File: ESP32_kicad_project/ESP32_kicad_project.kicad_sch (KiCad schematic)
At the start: 0 parts

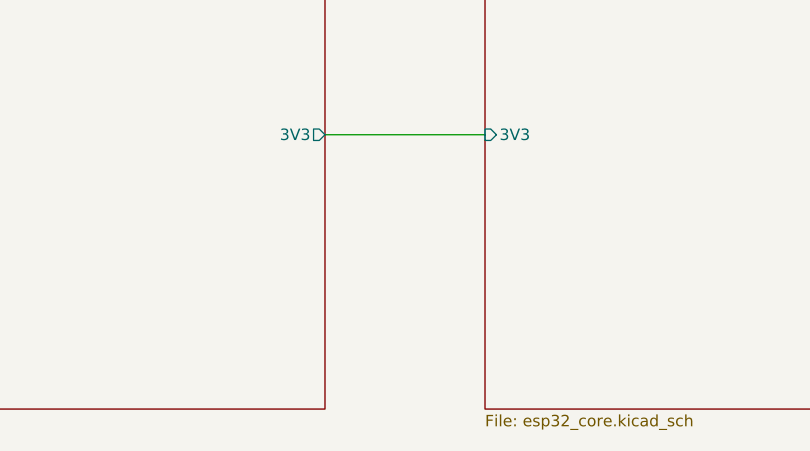
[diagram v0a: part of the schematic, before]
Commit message: added extra decoupling caps on the esp32 core 3V3 input
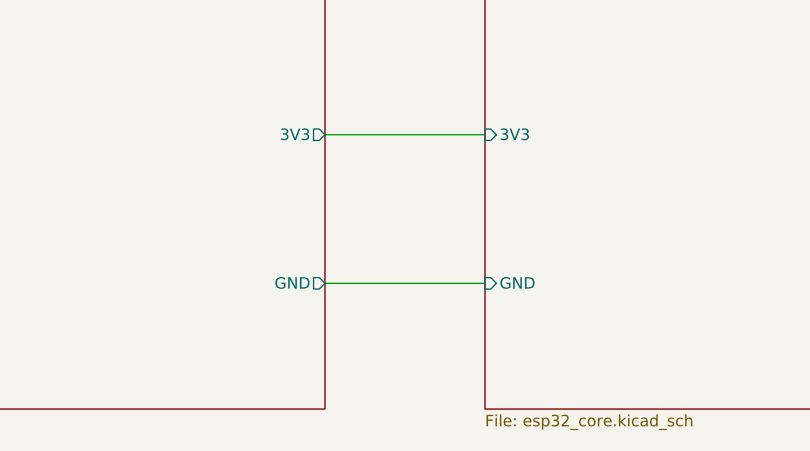
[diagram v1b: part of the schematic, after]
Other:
- sheet ESP32 Core ports: added GND; removed none
- sheet Power ports: added GND; removed none
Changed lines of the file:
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@@
+	(wire
+		(pts
+			(xy 93.98 62.23) (xy 111.76 62.23)
+		)
+		(stroke
+			(width 0)
+			(type default)
+		)
+	)
 	(wire
 		(pts
@@
 		(pin "3V3" input
 			(at 111.76 45.72 180)
+			(effects
+				(font
+					(size 1.27 1.27)
+				)
+				(justify left)
+			)
+		)
+		(pin "GND" input
+			(at 111.76 62.23 180)
 			(effects
 				(font
@@
 			(effects
 				(font
+					(size 1.27 1.27)
+				)
+				(justify right)
+			)
+		)
+		(pin "GND" output
+			(at 93.98 62.23 0)
+			(effects
+				(font

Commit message: completed core, moving on to the usb-uart core
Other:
- added sheet USB-UART (usb_uart.kicad_sch)
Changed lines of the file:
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@@
+		)
+	)
+	(sheet
+		(at 22.86 92.71)
+		(size 67.31 43.18)
+		(exclude_from_sim no)
+		(in_bom yes)
+		(on_board yes)
+		(dnp no)
+		(fields_autoplaced yes)
+		(stroke
+			(width 0.1524)
+			(type solid)
+		)
+		(fill
+			(color 0 0 0 0.0000)
+		)
+		(property "Sheetname" "USB-UART"
+			(at 22.86 91.9984 0)
+			(effects
+				(font
+					(size 1.27 1.27)
+				)
+				(justify left bottom)
+			)
+		)
+		(property "Sheetfile" "usb_uart.kicad_sch"
+			(at 22.86 136.4746 0)
+			(effects
+				(font
+					(size 1.27 1.27)
+				)
+				(justify left top)
+			)
+		)
+		(instances
+			(project "ESP32_kicad_project"
+				(path "/8f7d6ecf-e535-4443-9266-fe4b2e9314d5"
+					(page "4")
+				)
+			)
 		)
 	)

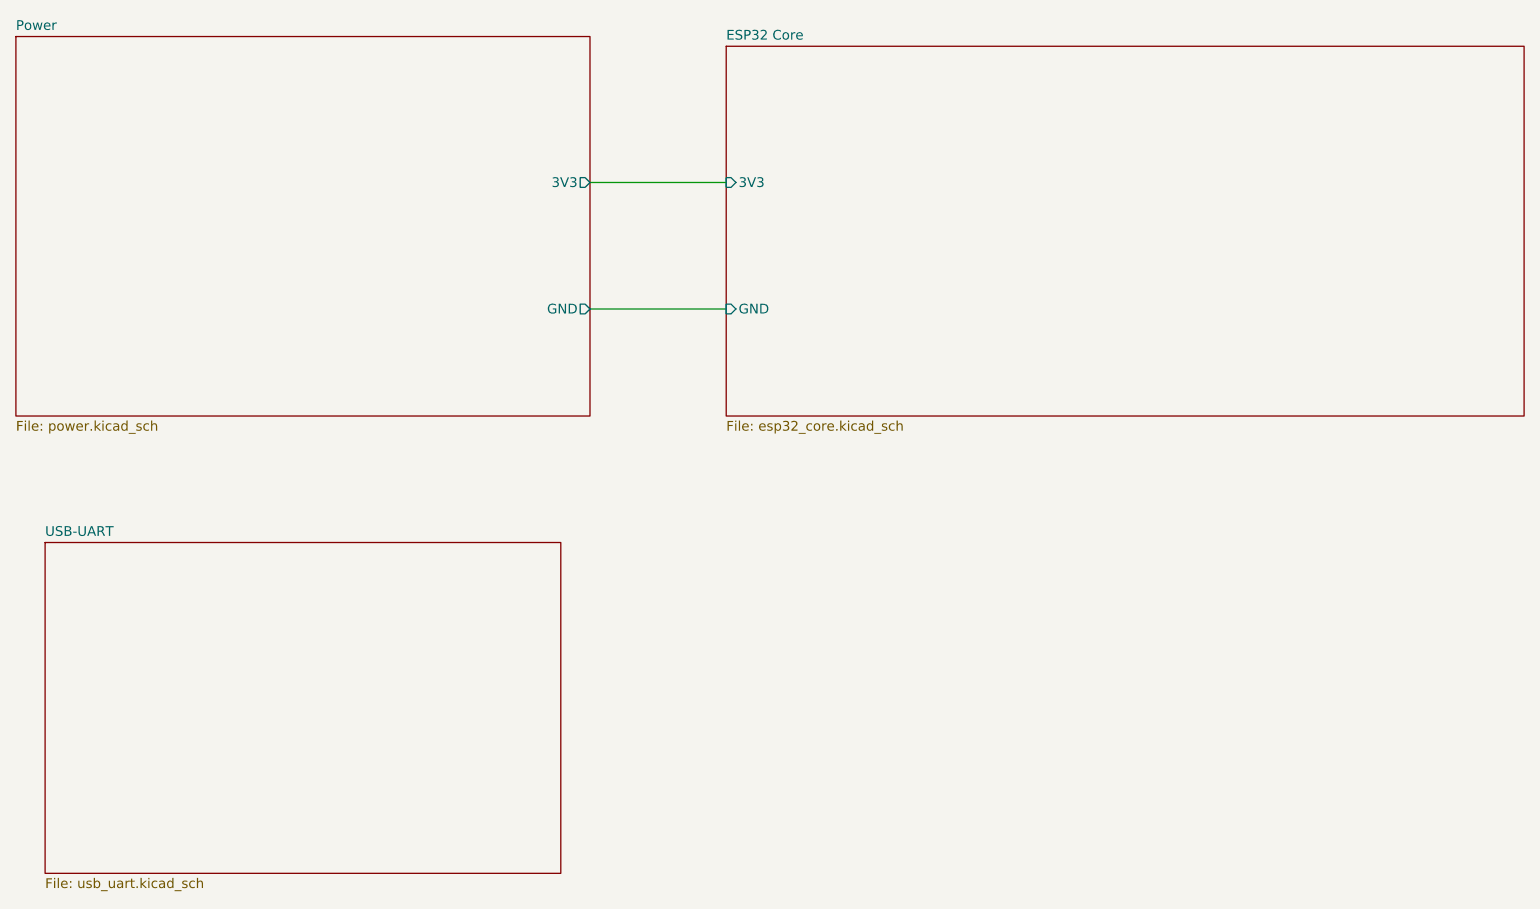
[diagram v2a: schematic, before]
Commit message: added USB chip, implemented ESP32 auto reset DTR RTS circuit
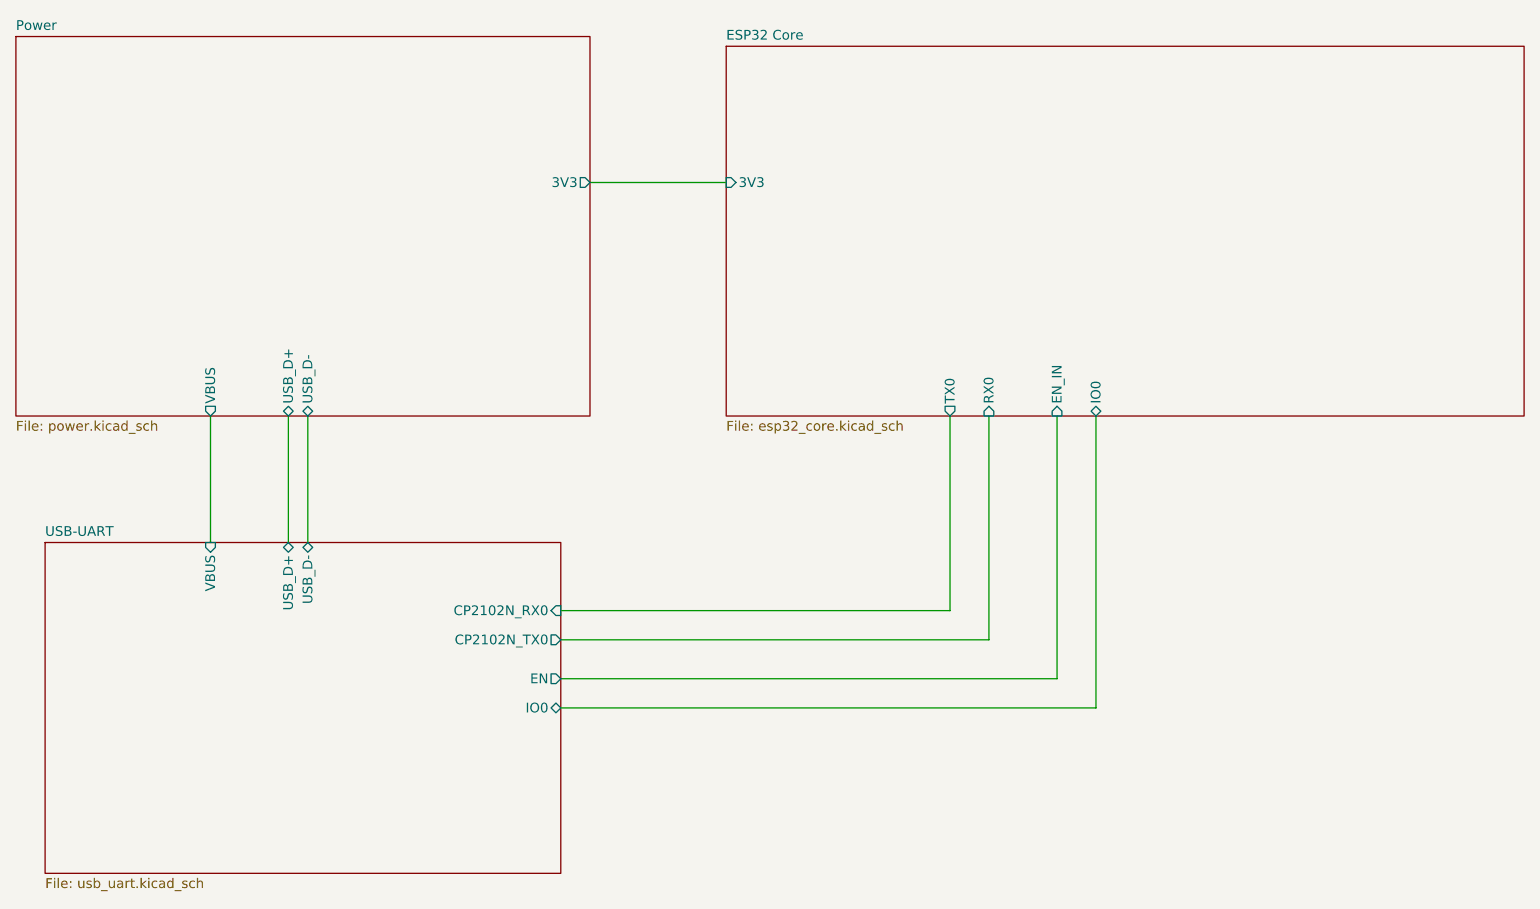
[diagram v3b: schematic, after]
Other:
- sheet ESP32 Core ports: added EN_IN, IO0, RX0, TX0; removed GND
- sheet Power ports: added USB_D+, USB_D-, VBUS; removed GND
- sheet USB-UART ports: added CP2102N_RX0, CP2102N_TX0, EN, IO0, USB_D+, USB_D-, VBUS; removed none
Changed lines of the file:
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@@
 	(wire
 		(pts
-			(xy 93.98 62.23) (xy 111.76 62.23)
+			(xy 160.02 76.2) (xy 160.02 114.3)
+		)
+		(stroke
+			(width 0)
+			(type default)
+		)
+	)
+	(wire
+		(pts
+			(xy 44.45 76.2) (xy 44.45 92.71)
+		)
+		(stroke
+			(width 0)
+			(type default)
+		)
+	)
+	(wire
+		(pts
+			(xy 154.94 76.2) (xy 154.94 110.49)
+		)
+		(stroke
+			(width 0)
+			(type default)
+		)
+	)
+	(wire
+		(pts
+			(xy 140.97 101.6) (xy 90.17 101.6)
+		)
+		(stroke
+			(width 0)
+			(type default)
+		)
+	)
+	(wire
+		(pts
+			(xy 146.05 105.41) (xy 90.17 105.41)
+		)
+		(stroke
+			(width 0)
+			(type default)
+		)
+	)
+	(wire
+		(pts
+			(xy 154.94 110.49) (xy 90.17 110.49)
+		)
+		(stroke
+			(width 0)
+			(type default)
+		)
+	)
+	(wire
+		(pts
+			(xy 160.02 114.3) (xy 90.17 114.3)
+		)
+		(stroke
+			(width 0)
+			(type default)
+		)
+	)
+	(wire
+		(pts
+			(xy 140.97 76.2) (xy 140.97 101.6)
+		)
+		(stroke
+			(width 0)
+			(type default)
+		)
+	)
+	(wire
+		(pts
+			(xy 57.15 76.2) (xy 57.15 92.71)
+		)
+		(stroke
+			(width 0)
+			(type default)
+		)
+	)
+	(wire
+		(pts
+			(xy 146.05 76.2) (xy 146.05 105.41)
 		)
 		(stroke
@@
 		(pts
 			(xy 93.98 45.72) (xy 111.76 45.72)
+		)
+		(stroke
+			(width 0)
+			(type default)
+		)
+	)
+	(wire
+		(pts
+			(xy 54.61 76.2) (xy 54.61 92.71)
 		)
 		(stroke
@@
 			)
 		)
-		(pin "GND" input
-			(at 111.76 62.23 180)
+		(pin "TX0" output
+			(at 140.97 76.2 270)
+			(effects
+				(font
+					(size 1.27 1.27)
+				)
+				(justify left)
+			)
+		)
+		(pin "RX0" input
+			(at 146.05 76.2 270)
+			(effects
+				(font
+					(size 1.27 1.27)
+				)
+				(justify left)
+			)
+		)
+		(pin "IO0" bidirectional
+			(at 160.02 76.2 270)
+			(effects
+				(font
+					(size 1.27 1.27)
+				)
+				(justify left)
+			)
+		)
+		(pin "EN_IN" input
+			(at 154.94 76.2 270)
 			(effects
 				(font
@@
 			)
 		)
-		(pin "GND" output
-			(at 93.98 62.23 0)
-			(effects
-				(font
-					(size 1.27 1.27)
-				)
-				(justify right)
+		(pin "VBUS" output
+			(at 44.45 76.2 270)
+			(effects
+				(font
+					(size 1.27 1.27)
+				)
+				(justify left)
+			)
+		)
+		(pin "USB_D+" bidirectional
+			(at 54.61 76.2 270)
+			(effects
+				(font
+					(size 1.27 1.27)
+				)
+				(justify left)
+			)
+		)
+		(pin "USB_D-" bidirectional
+			(at 57.15 76.2 270)
+			(effects
+				(font
+					(size 1.27 1.27)
+				)
+				(justify left)
 			)
 		)
@@
 			)
 		)
+		(pin "VBUS" input
+			(at 44.45 92.71 90)
+			(effects
+				(font
+					(size 1.27 1.27)
+				)
+				(justify right)
+			)
+		)
+		(pin "USB_D-" bidirectional
+			(at 57.15 92.71 90)
+			(effects
+				(font
+					(size 1.27 1.27)
+				)
+				(justify right)
+			)
+		)
+		(pin "USB_D+" bidirectional
+			(at 54.61 92.71 90)
+			(effects
+				(font
+					(size 1.27 1.27)
+				)
+				(justify right)
+			)
+		)
+		(pin "CP2102N_RX0" input
+			(at 90.17 101.6 0)
+			(effects
+				(font
+					(size 1.27 1.27)
+				)
+				(justify right)
+			)
+		)
+		(pin "CP2102N_TX0" output
+			(at 90.17 105.41 0)
+			(effects
+				(font
+					(size 1.27 1.27)
+				)
+				(justify right)
+			)
+		)
+		(pin "EN" output
+			(at 90.17 110.49 0)
+			(effects
+				(font
+					(size 1.27 1.27)
+				)
+				(justify right)
+			)
+		)
+		(pin "IO0" bidirectional
+			(at 90.17 114.3 0)
+			(effects
+				(font
+					(size 1.27 1.27)
+				)
+				(justify right)
+			)
+		)

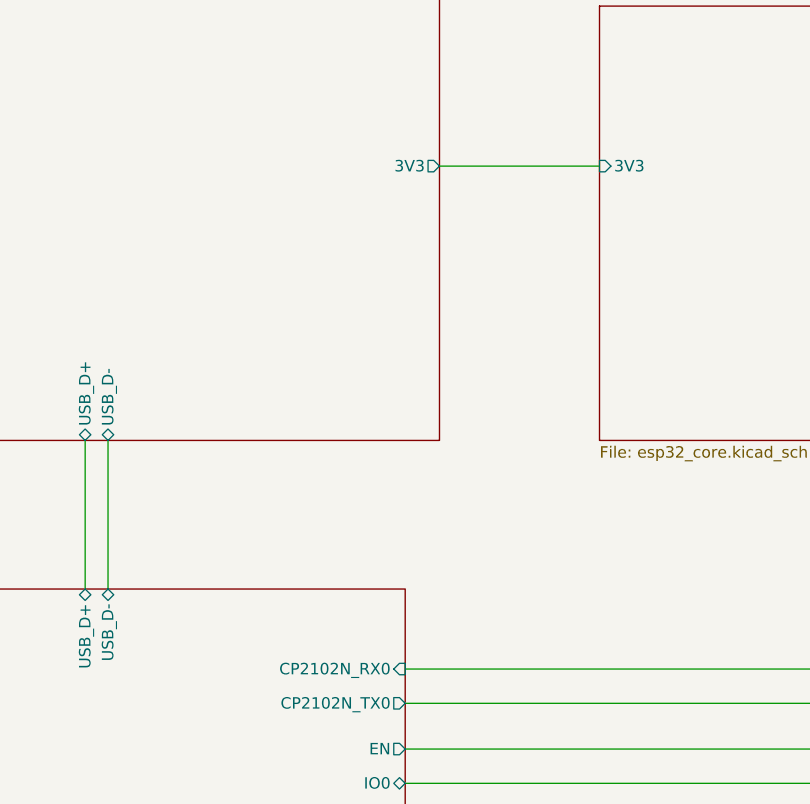
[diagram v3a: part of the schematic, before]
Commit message: completed USB-UART, created GPIO pin connectors, completed schematic work. moving on to PCB
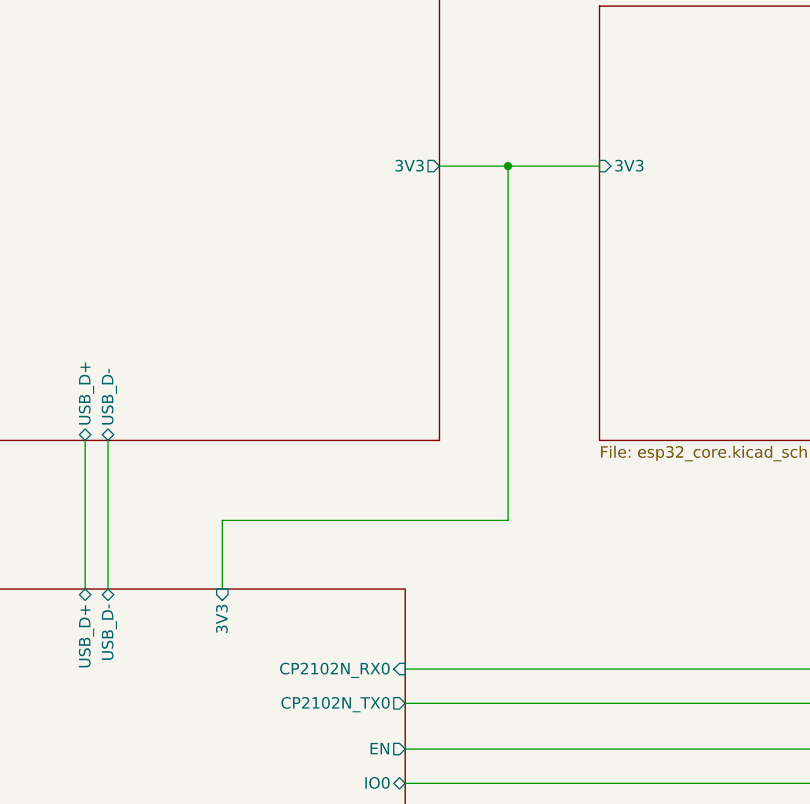
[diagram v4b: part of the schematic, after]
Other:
- sheet USB-UART ports: added 3V3; removed none
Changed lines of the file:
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@@
 	(generator_version "9.0")
 	(paper "A4")
+	(junction
+		(at 101.6 45.72)
+		(diameter 0)
+		(color 0 0 0 0)
+	)
 	(wire
 		(pts
@@
 	(wire
 		(pts
+			(xy 69.85 85.09) (xy 101.6 85.09)
+		)
+		(stroke
+			(width 0)
+			(type default)
+		)
+	)
+	(wire
+		(pts
 			(xy 160.02 114.3) (xy 90.17 114.3)
 		)
@@
 	(wire
 		(pts
+			(xy 101.6 45.72) (xy 111.76 45.72)
+		)
+		(stroke
+			(width 0)
+			(type default)
+		)
+	)
+	(wire
+		(pts
 			(xy 57.15 76.2) (xy 57.15 92.71)
 		)
@@
 	(wire
 		(pts
-			(xy 93.98 45.72) (xy 111.76 45.72)
+			(xy 93.98 45.72) (xy 101.6 45.72)
 		)
 		(stroke
@@
 		(pts
 			(xy 54.61 76.2) (xy 54.61 92.71)
+		)
+		(stroke
+			(width 0)
+			(type default)
+		)
+	)
+	(wire
+		(pts
+			(xy 69.85 92.71) (xy 69.85 85.09)
+		)
+		(stroke
+			(width 0)
+			(type default)
+		)
+	)
+	(wire
+		(pts
+			(xy 101.6 85.09) (xy 101.6 45.72)
 		)
 		(stroke
@@
 			(effects
 				(font
+					(size 1.27 1.27)
+				)
+				(justify right)
+			)
+		)
+		(pin "3V3" input
+			(at 69.85 92.71 90)
+			(effects
+				(font

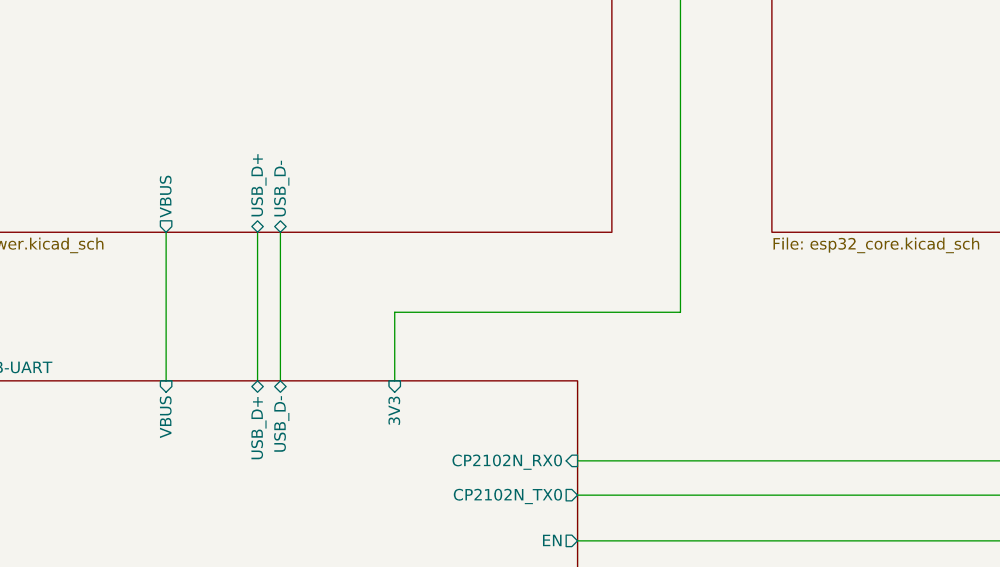
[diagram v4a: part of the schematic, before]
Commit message: completed schematic design, replaced regulator output inductor with a smaller part, fit components in a board in PCB editor, will start routing
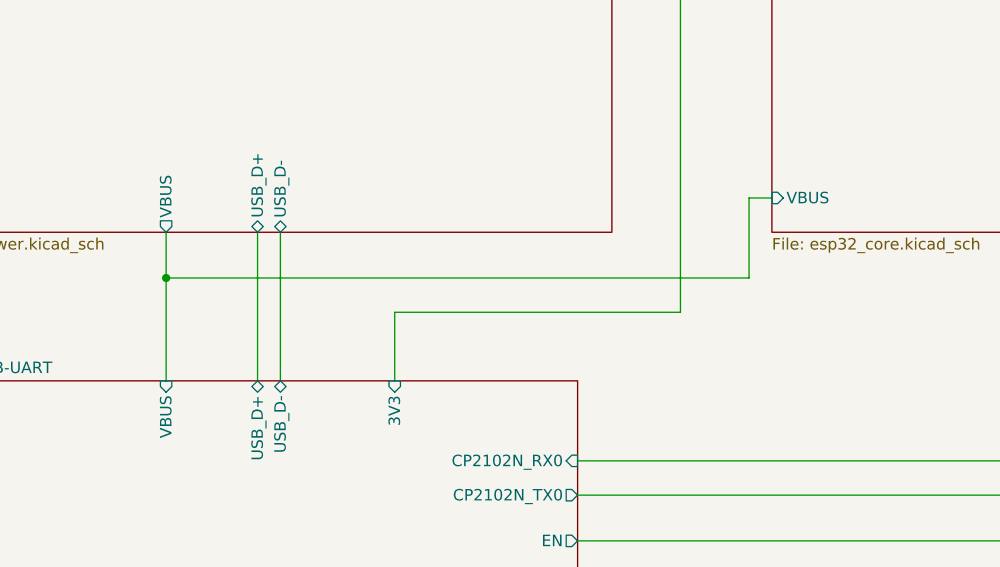
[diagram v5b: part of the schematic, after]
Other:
- sheet ESP32 Core ports: added VBUS; removed none
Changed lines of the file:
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@@
 		(color 0 0 0 0)
 	)
+	(junction
+		(at 44.45 81.28)
+		(diameter 0)
+		(color 0 0 0 0)
+	)
 	(wire
 		(pts
@@
 	(wire
 		(pts
-			(xy 44.45 76.2) (xy 44.45 92.71)
+			(xy 44.45 76.2) (xy 44.45 81.28)
 		)
 		(stroke
@@
 	(wire
 		(pts
+			(xy 44.45 81.28) (xy 109.22 81.28)
+		)
+		(stroke
+			(width 0)
+			(type default)
+		)
+	)
+	(wire
+		(pts
 			(xy 69.85 85.09) (xy 101.6 85.09)
 		)
@@
 	(wire
 		(pts
+			(xy 44.45 81.28) (xy 44.45 92.71)
+		)
+		(stroke
+			(width 0)
+			(type default)
+		)
+	)
+	(wire
+		(pts
 			(xy 57.15 76.2) (xy 57.15 92.71)
 		)
@@
 		(pts
 			(xy 101.6 85.09) (xy 101.6 45.72)
+		)
+		(stroke
+			(width 0)
+			(type default)
+		)
+	)
+	(wire
+		(pts
+			(xy 109.22 72.39) (xy 109.22 81.28)
+		)
+		(stroke
+			(width 0)
+			(type default)
+		)
+	)
+	(wire
+		(pts
+			(xy 111.76 72.39) (xy 109.22 72.39)
 		)
 		(stroke
@@
 			(effects
 				(font
+					(size 1.27 1.27)
+				)
+				(justify left)
+			)
+		)
+		(pin "VBUS" input
+			(at 111.76 72.39 180)
+			(effects
+				(font
